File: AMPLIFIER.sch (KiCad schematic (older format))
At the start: 29 parts

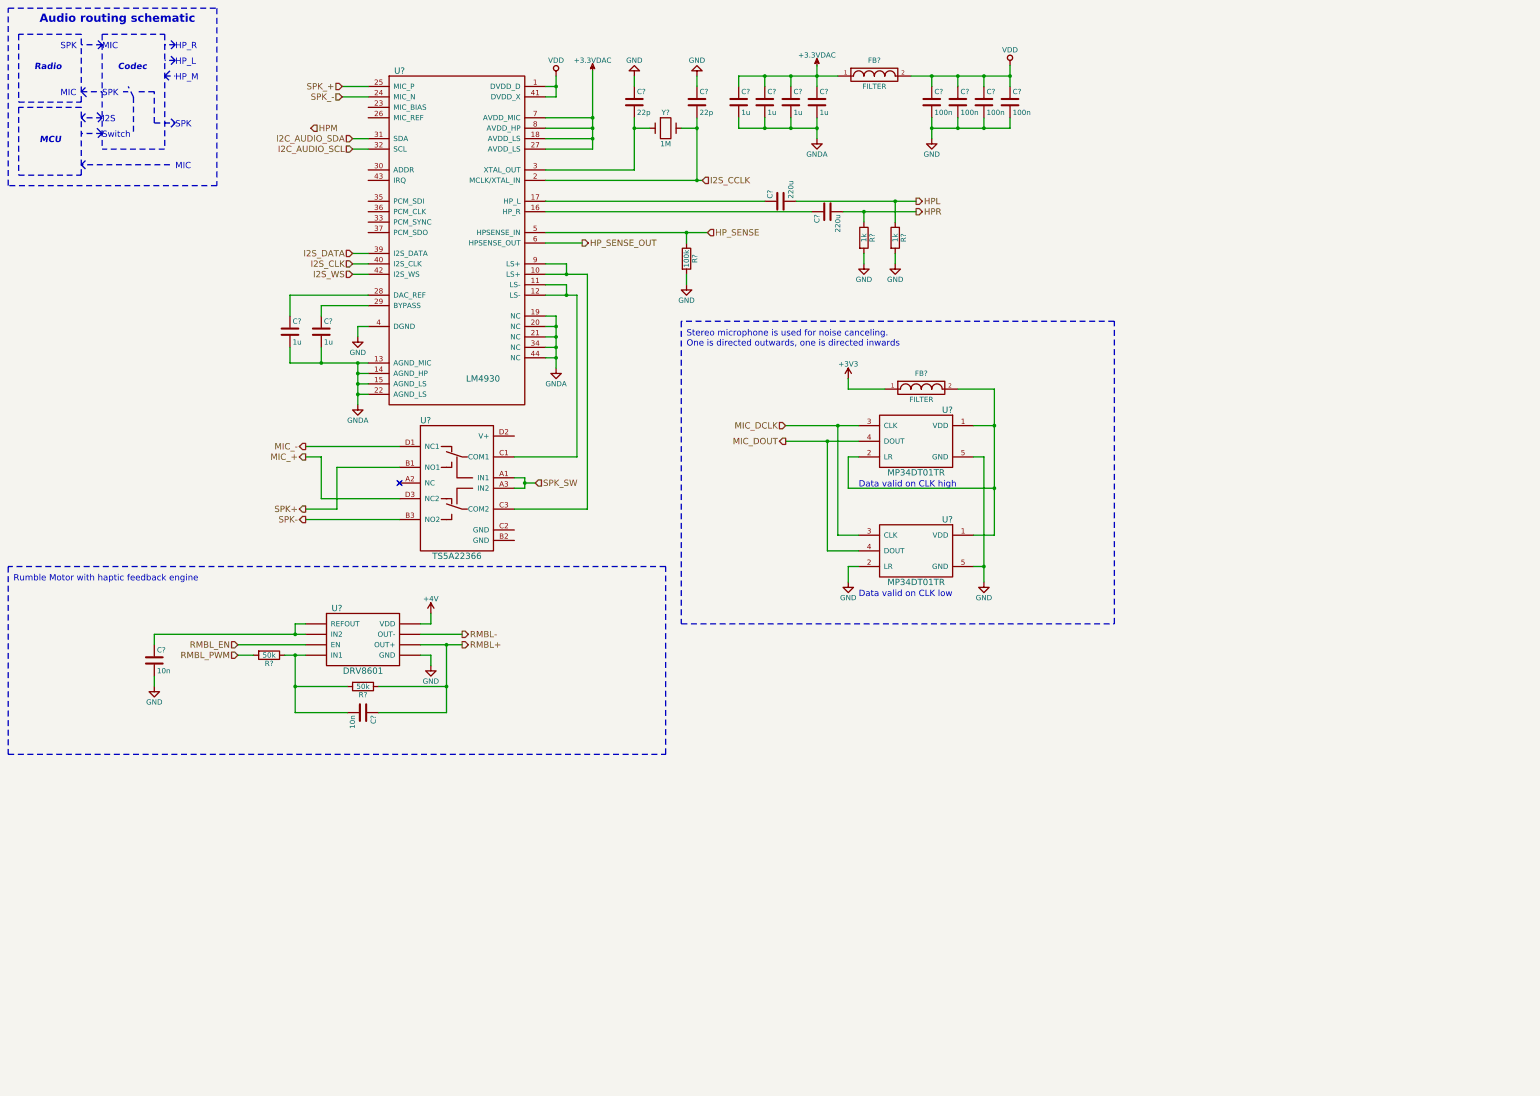
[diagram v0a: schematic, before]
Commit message: Removed WiFi Module added Footprints
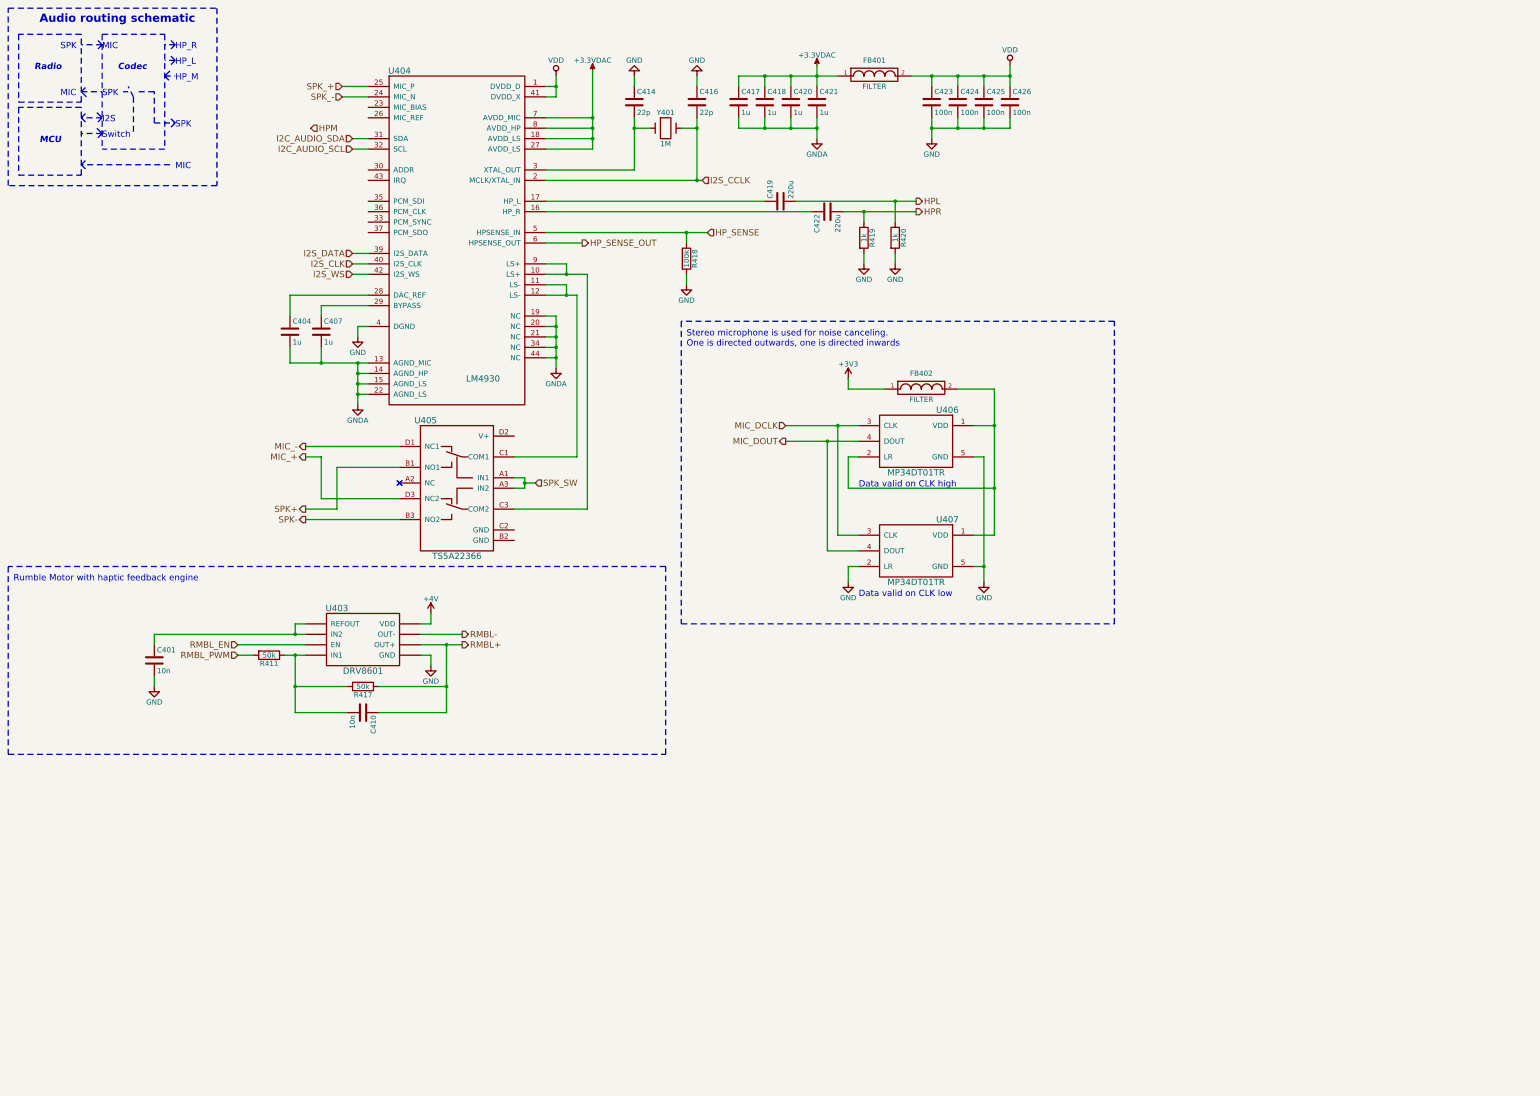
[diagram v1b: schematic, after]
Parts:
- C401, C404, C407, C410, C414, C416, C417, C418, C419, C420, C421, C422, C423, C424, C425, C426: renamed from C?; footprint (none) -> Capacitors_SMD:C_0603
- FB401, FB402: renamed from FB?; footprint (none) -> Choke_SMD:Choke_SMD_1206_Standard
- R411, R417, R418, R419, R420: renamed from R?; footprint (none) -> Resistors_SMD:R_0603
- U403: renamed from U?; footprint (none) -> buttons:DRV8601
- U404: renamed from U?; footprint (none) -> Housings_DFN_QFN:QFN-44-1EP_7x7mm_Pitch0.5mm
- U405: renamed from U?; footprint (none) -> buttons:TS5A22366
- U406, U407: renamed from U?; footprint (none) -> buttons:MP34DT01
- Y401: renamed from Y?; footprint (none) -> Crystals:Crystal_SMD_SeikoEpson_MC146-4pin_6.7x1.5mm_HandSoldering

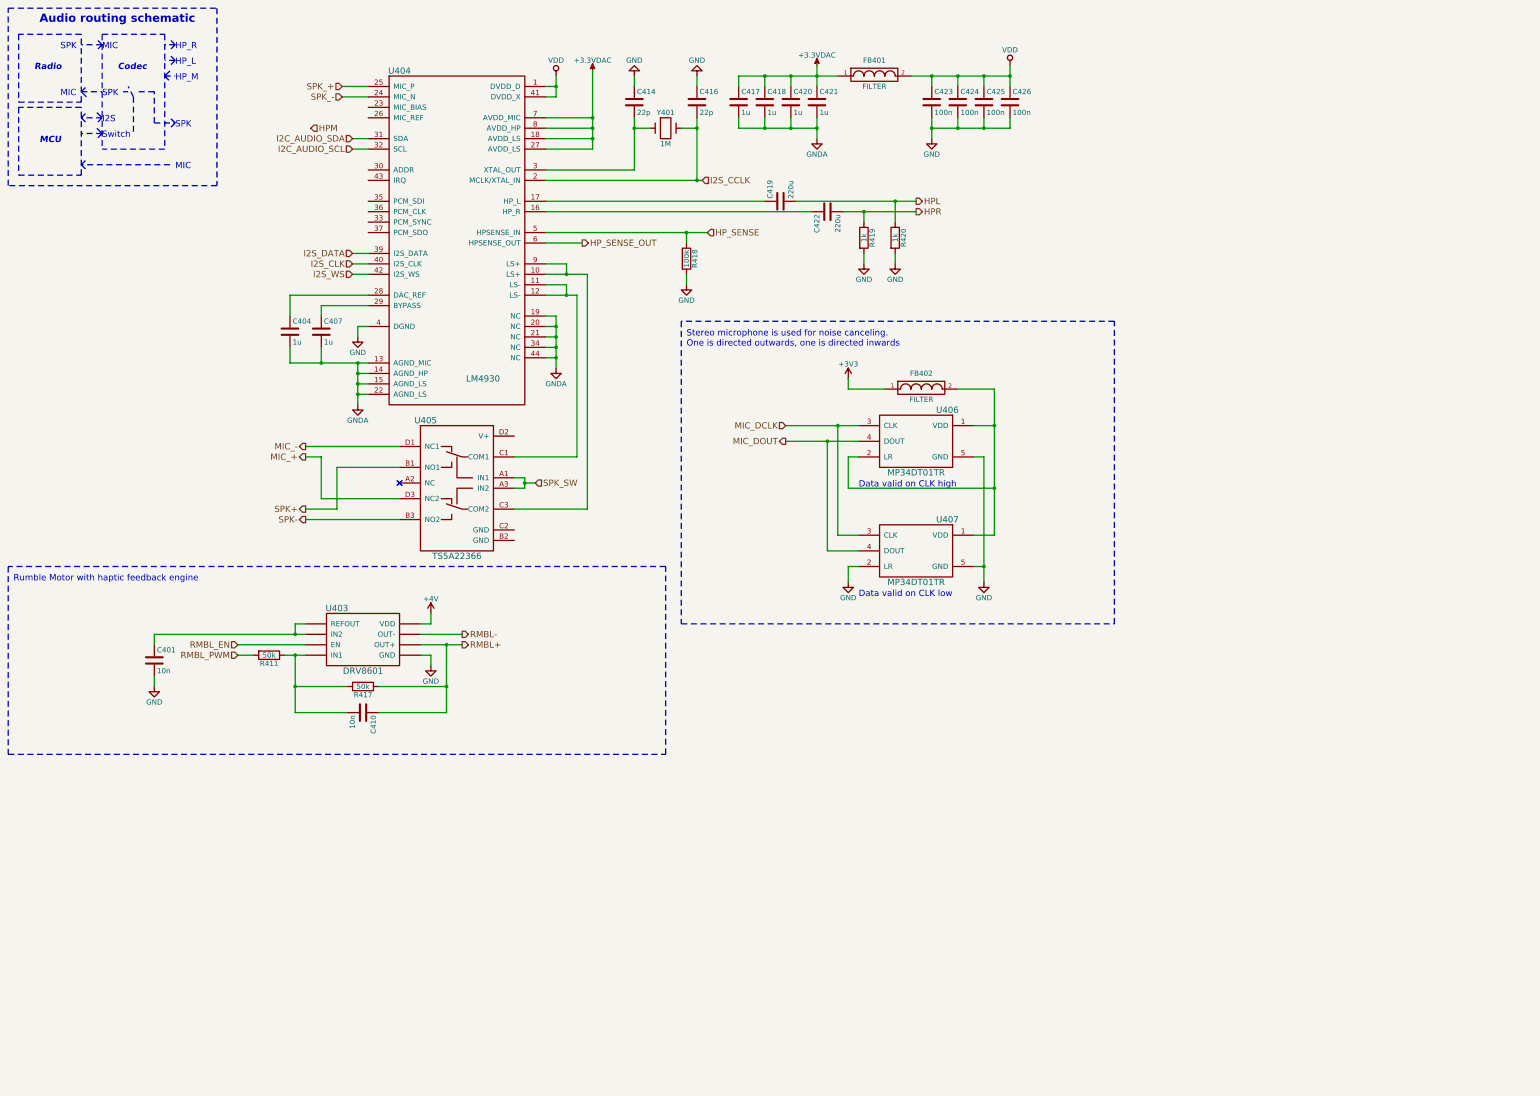
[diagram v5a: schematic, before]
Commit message: Connected WIFI subsheet with ESP8266 and WL1807MOD to SD2 Connected WL1807MOD Bluetoth UART to UART3 Connected A7 Module AT UART to UART6 Connected A7 GPS UART to UART5 Connected A7 HS download to UART7 Connected debug pins to UART1 Connected debug pins to UART2 Added CPU_PWR subsheet to connect power rails to i.MX7 A7 UARTs are routed through level shifter to get from 2.8V to 3.3V All the sheets should be on A3 size now Externel USB is connected to USB_OTG1 Board power sheet is cleared out. Only 4V booster is needed.
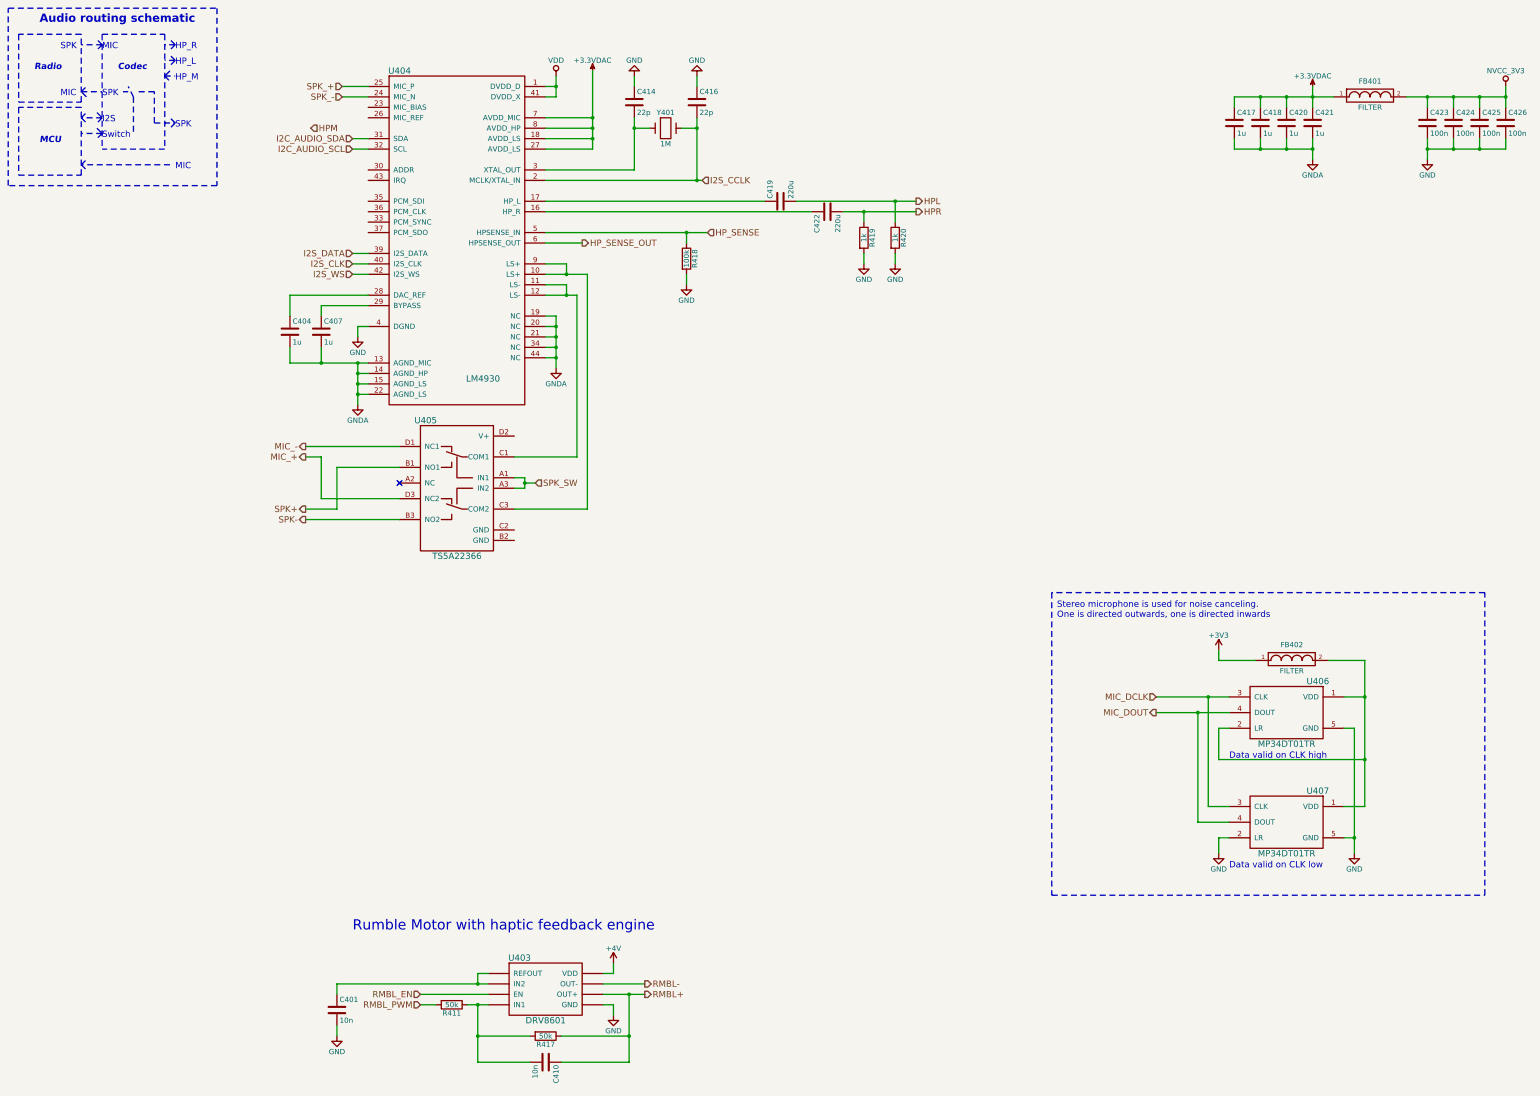
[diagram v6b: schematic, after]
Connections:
- net VDD: no longer C423.1, C424.1, C425.1, C426.1, FB401.2
- new net NVCC_3V3: C423.1, C424.1, C425.1, C426.1, FB401.2
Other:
- moved on the sheet: C401, C410, C417, C418, C420, C421, C423, C424, C425, C426, FB401, FB402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
